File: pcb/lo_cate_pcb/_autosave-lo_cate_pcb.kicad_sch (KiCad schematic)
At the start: 42 parts, among them J1 Conn_01x07_Pin, J2 690-005-299-043, SW1 MICRO_RESET, SW2 MICRO_ON, SW3 BUTTON1, SW4 BUTTON2, SW5 BUTTON3, U1 STM32F401RETx, U2 BMI323, U3 150141M173100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

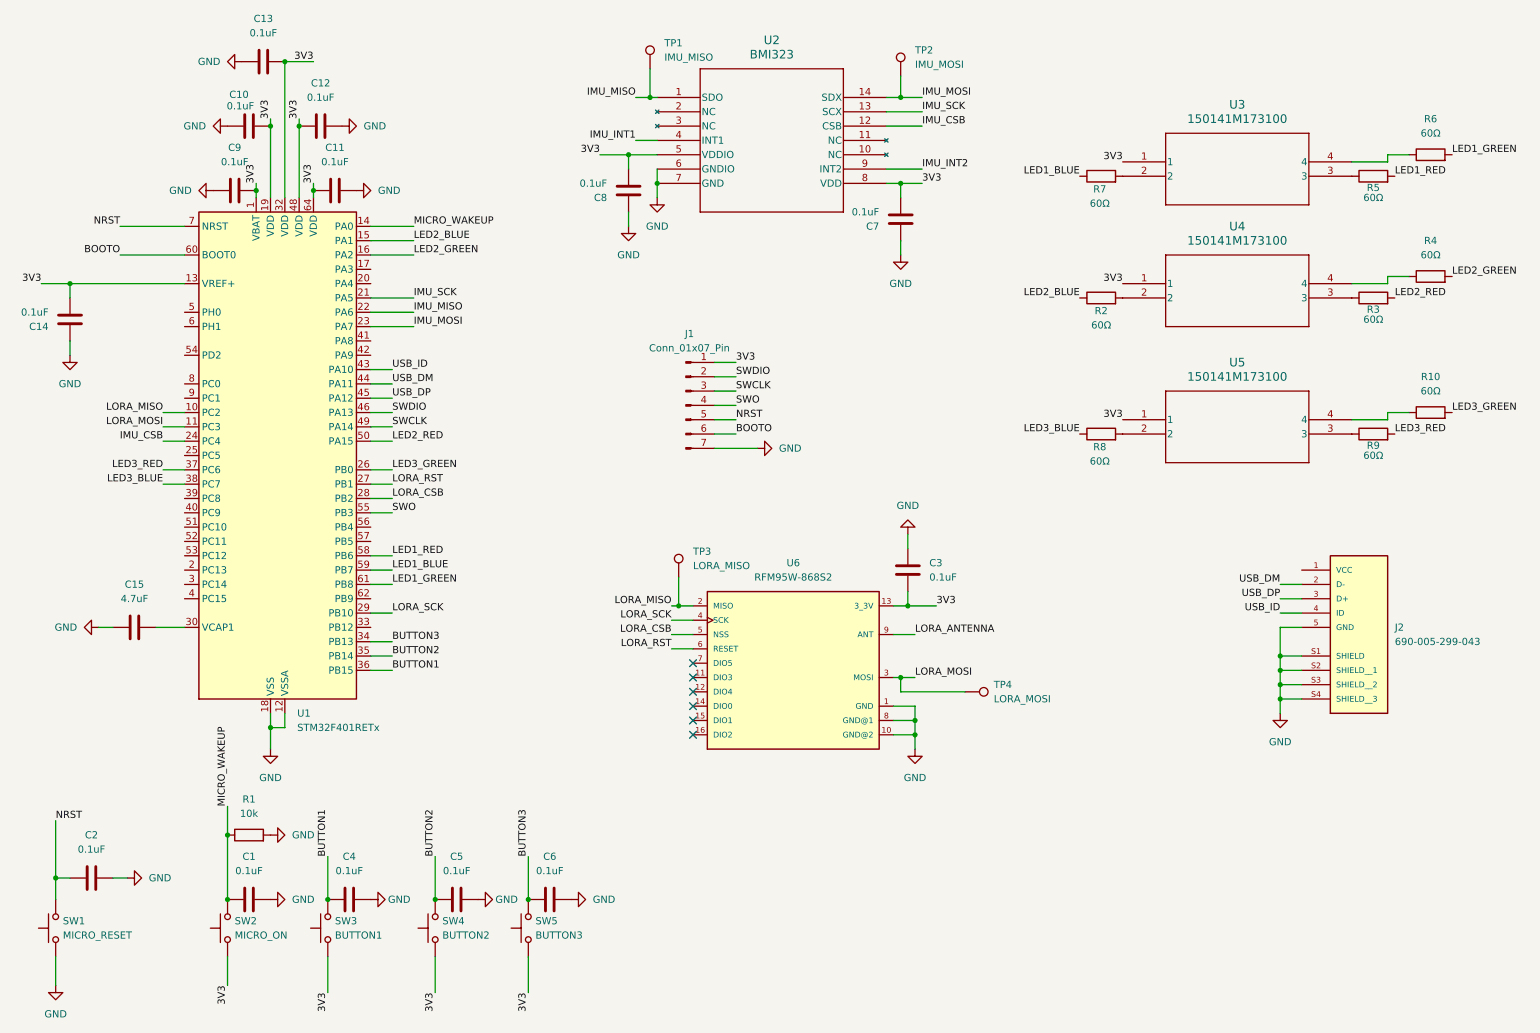
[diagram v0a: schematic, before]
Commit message: USB connector added to pcb, All that is left is power electronics and antenna
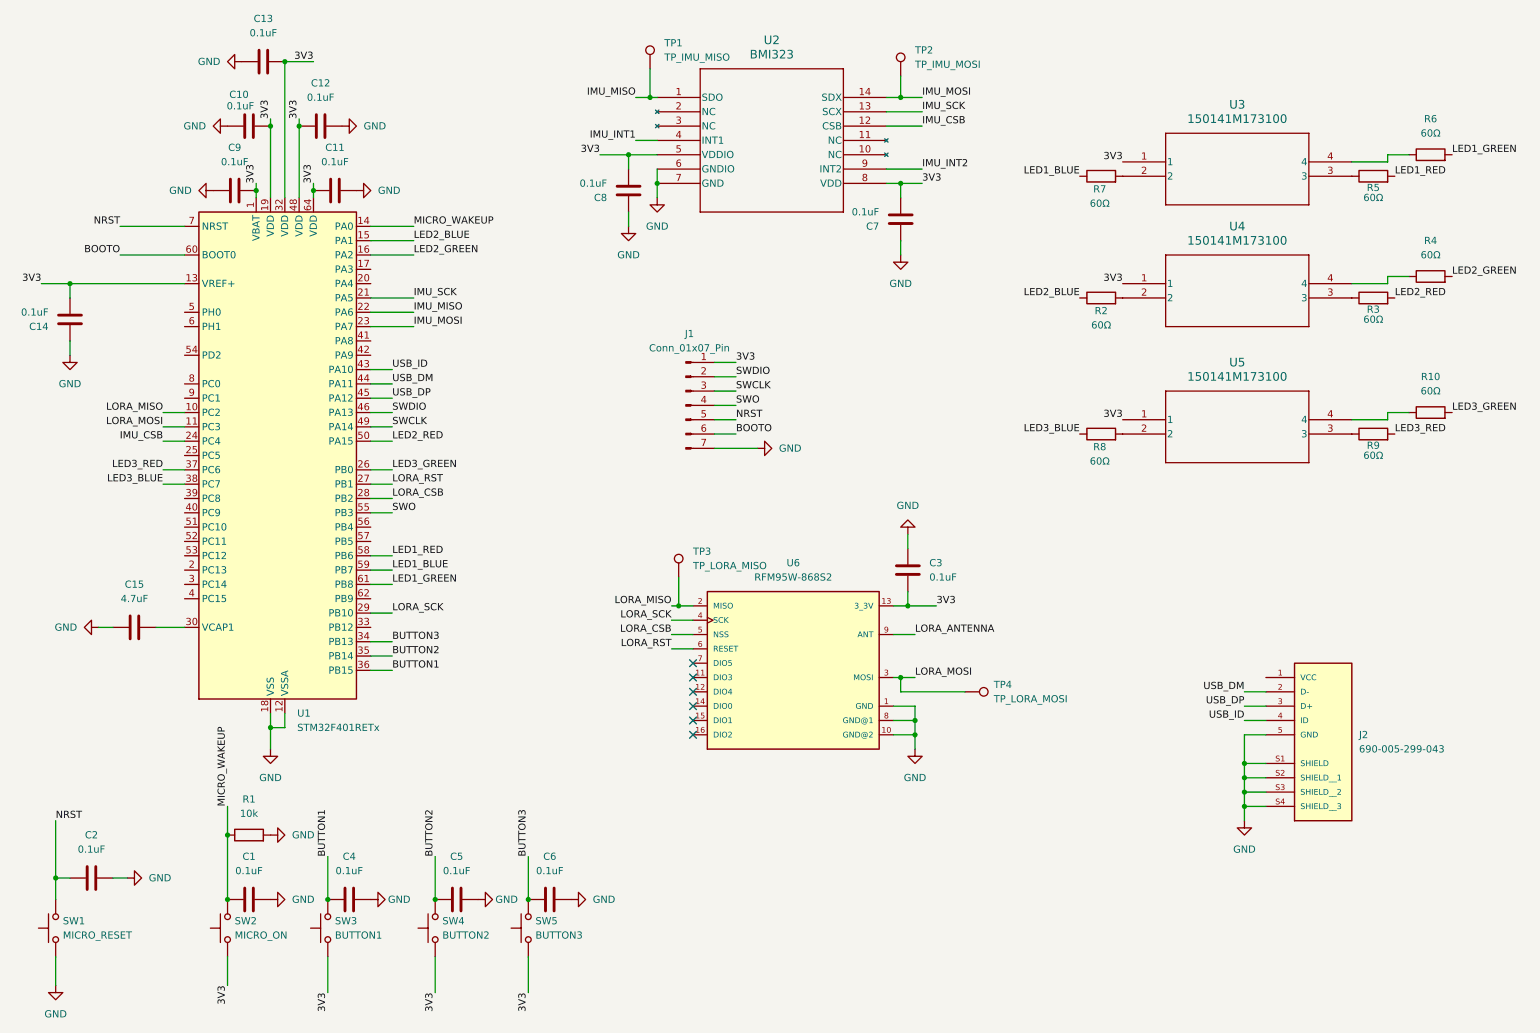
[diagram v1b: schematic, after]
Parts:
- J2: footprint 690-005-299-043:EDAC_690-005-299-043 -> footprints:EDAC_690-005-299-043
- TP1: value IMU_MISO -> TP_IMU_MISO; footprint (none) -> TestPoint:TestPoint_Pad_D2.5mm
- TP2: value IMU_MOSI -> TP_IMU_MOSI; footprint (none) -> TestPoint:TestPoint_Pad_D2.5mm
- TP3: value LORA_MISO -> TP_LORA_MISO; footprint (none) -> TestPoint:TestPoint_Pad_D2.5mm
- TP4: value LORA_MOSI -> TP_LORA_MOSI; footprint (none) -> footprints:EDAC_690-005-299-043
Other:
- moved on the sheet: J2
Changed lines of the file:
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@@
 	)
 	(junction
-		(at 241.3 134.62)
+		(at 234.95 153.67)
 		(diameter 0)
 		(color 0 0 0 0)
@@
 	)
 	(junction
-		(at 241.3 137.16)
+		(at 234.95 156.21)
 		(diameter 0)
 		(color 0 0 0 0)
@@
 	)
 	(junction
-		(at 241.3 132.08)
+		(at 234.95 151.13)
 		(diameter 0)
 		(color 0 0 0 0)
@@
 	)
 	(junction
-		(at 241.3 129.54)
+		(at 234.95 148.59)
 		(diameter 0)
 		(color 0 0 0 0)
@@
 	(wire
 		(pts
-			(xy 241.3 137.16) (xy 245.11 137.16)
+			(xy 234.95 156.21) (xy 238.76 156.21)
 		)
 		(stroke
@@
 	(wire
 		(pts
-			(xy 241.3 129.54) (xy 245.11 129.54)
+			(xy 234.95 148.59) (xy 238.76 148.59)
 		)
 		(stroke
@@
 	(wire
 		(pts
-			(xy 245.11 121.92) (xy 241.3 121.92)
+			(xy 238.76 140.97) (xy 234.95 140.97)
 		)
 		(stroke
@@
 	(wire
 		(pts
-			(xy 245.11 124.46) (xy 241.3 124.46)
+			(xy 238.76 143.51) (xy 234.95 143.51)
 		)
 		(stroke
@@
 	(wire
 		(pts
-			(xy 245.11 119.38) (xy 241.3 119.38)
+			(xy 238.76 138.43) (xy 234.95 138.43)
 		)
 		(stroke
@@
 	(wire
 		(pts
-			(xy 245.11 132.08) (xy 241.3 132.08)
+			(xy 238.76 151.13) (xy 234.95 151.13)
 		)
 		(stroke
@@
 	(wire
 		(pts
-			(xy 241.3 134.62) (xy 245.11 134.62)
+			(xy 234.95 153.67) (xy 238.76 153.67)
 		)
 		(stroke
@@
 	(wire
 		(pts
-			(xy 241.3 129.54) (xy 241.3 132.08)
+			(xy 234.95 148.59) (xy 234.95 151.13)
 		)
 		(stroke
@@
 	(wire
 		(pts
-			(xy 245.11 116.84) (xy 241.3 116.84)
+			(xy 238.76 135.89) (xy 234.95 135.89)
 		)
 		(stroke
@@
 	(wire
 		(pts
-			(xy 241.3 132.08) (xy 241.3 134.62)
+			(xy 234.95 151.13) (xy 234.95 153.67)
 		)
 		(stroke
@@
 	(wire
 		(pts
-			(xy 241.3 137.16) (xy 241.3 139.7)
+			(xy 234.95 156.21) (xy 234.95 158.75)
 		)
 		(stroke
@@
 	(wire
 		(pts
-			(xy 241.3 124.46) (xy 241.3 129.54)
+			(xy 234.95 143.51) (xy 234.95 148.59)
 		)
 		(stroke
@@
 	(wire
 		(pts
-			(xy 241.3 134.62) (xy 241.3 137.16)
+			(xy 234.95 153.67) (xy 234.95 156.21)
 		)
 		(stroke
@@
 	)
 	(label "USB_DM"
-		(at 241.3 116.84 180)
+		(at 234.95 135.89 180)
 		(fields_autoplaced yes)
 		(effects
@@
 	)
 	(label "USB_DP"
-		(at 241.3 119.38 180)
+		(at 234.95 138.43 180)
 		(fields_autoplaced yes)
 		(effects
@@
 	)
 	(label "USB_ID"
-		(at 241.3 121.92 180)
+		(at 234.95 140.97 180)
 		(fields_autoplaced yes)
 		(effects
@@
 			)
 		)
-		(property "Value" "LORA_MISO"
+		(property "Value" "TP_LORA_MISO"
 			(at 137.16 113.5379 0)
 			(effects
@@
 			)
 		)
-		(property "Footprint" ""
+		(property "Footprint" "TestPoint:TestPoint_Pad_D2.5mm"
 			(at 139.7 115.57 0)
 			(effects
@@
 			)
 		)
-		(property "Value" "IMU_MISO"
+		(property "Value" "TP_IMU_MISO"
 			(at 132.08 23.3679 0)
 			(effects
@@
 			)
 		)
-		(property "Footprint" ""
+		(property "Footprint" "TestPoint:TestPoint_Pad_D2.5mm"
 			(at 134.62 25.4 0)
 			(effects
@@
 			)
 		)
-		(property "Value" "IMU_MOSI"
+		(property "Value" "TP_IMU_MOSI"
 			(at 176.53 24.6379 0)
 			(effects
@@
 			)
 		)
-		(property "Footprint" ""
+		(property "Footprint" "TestPoint:TestPoint_Pad_D2.5mm"
 			(at 179.07 26.67 0)
 			(effects
@@
 	(symbol
 		(lib_id "690-005-299-043:690-005-299-043")
-		(at 255.27 121.92 0)
+		(at 248.92 140.97 0)
 		(unit 1)
 		(exclude_from_sim no)
@@
 		(fields_autoplaced yes)
 		(property "Reference" "J2"
-			(at 261.62 124.4599 0)
+			(at 255.27 143.5099 0)
 			(effects
 				(font
@@
 		)
 		(property "Value" "690-005-299-043"
-			(at 261.62 126.9999 0)
+			(at 255.27 146.0499 0)
 			(effects
 				(font
@@
 			)
 		)
-		(property "Footprint" "690-005-299-043:EDAC_690-005-299-043"
-			(at 255.27 121.92 0)
+		(property "Footprint" "footprints:EDAC_690-005-299-043"
+			(at 248.92 140.97 0)
 			(effects
 				(font
@@
 		)
 		(property "Datasheet" ""
-			(at 255.27 121.92 0)
+			(at 248.92 140.97 0)
 			(effects
 				(font
@@
 		)
 		(property "Description" ""
-			(at 255.27 121.92 0)
+			(at 248.92 140.97 0)
 			(effects
 				(font
@@
 		)
 		(property "PARTREV" "11"
-			(at 255.27 121.92 0)
+			(at 248.92 140.97 0)
 			(effects
 				(font
@@
 		)
 		(property "MANUFACTURER" "EDAC"
-			(at 255.27 121.92 0)
+			(at 248.92 140.97 0)
 			(effects
 				(font
@@
 		)
 		(property "MAXIMUM_PACKAGE_HEIGHT" "3.98mm"
-			(at 255.27 121.92 0)
+			(at 248.92 140.97 0)
 			(effects
 				(font
@@
 		)
 		(property "STANDARD" "Manufacturer Recommendations"
-			(at 255.27 121.92 0)
+			(at 248.92 140.97 0)
 			(effects
 				(font
@@
 	(symbol
 		(lib_id "power:GND")
-		(at 241.3 139.7 0)
+		(at 234.95 158.75 0)
 		(unit 1)
 		(exclude_from_sim no)
@@
 		(fields_autoplaced yes)
 		(property "Reference" "#PWR022"
-			(at 241.3 146.05 0)
+			(at 234.95 165.1 0)
 			(effects
 				(font
@@
 		)
 		(property "Value" "GND"
-			(at 241.3 144.78 0)
+			(at 234.95 163.83 0)
 			(effects
 				(font
@@
 		)
 		(property "Footprint" ""
-			(at 241.3 139.7 0)
+			(at 234.95 158.75 0)
 			(effects
 				(font
@@
 		)
 		(property "Datasheet" ""
-			(at 241.3 139.7 0)
+			(at 234.95 158.75 0)
 			(effects
 				(font
@@
 		)
 		(property "Description" "Power symbol creates a global label with name \"GND\" , ground"
-			(at 241.3 139.7 0)
+			(at 234.95 158.75 0)
 			(effects
 				(font
@@
 			)
 		)
-		(property "Value" "LORA_MOSI"
+		(property "Value" "TP_LORA_MOSI"
 			(at 190.5 137.1599 90)
 			(effects
@@
 			)
 		)
-		(property "Footprint" ""
+		(property "Footprint" "footprints:EDAC_690-005-299-043"
 			(at 185.42 140.97 0)
 			(effects
